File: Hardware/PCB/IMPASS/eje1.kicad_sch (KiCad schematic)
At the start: 18 parts, among them Q1 BC847BDW1, Q2 DMP3013SFV, Q3 DMP3013SFV, Q4 DMP3013SFV, Q5 BC847BDW1, Q6 DMP3013SFV, Q71 DMN3008SFG, Q73 DMN3008SFG, Q75 DMN3008SFG, Q77 DMN3008SFG

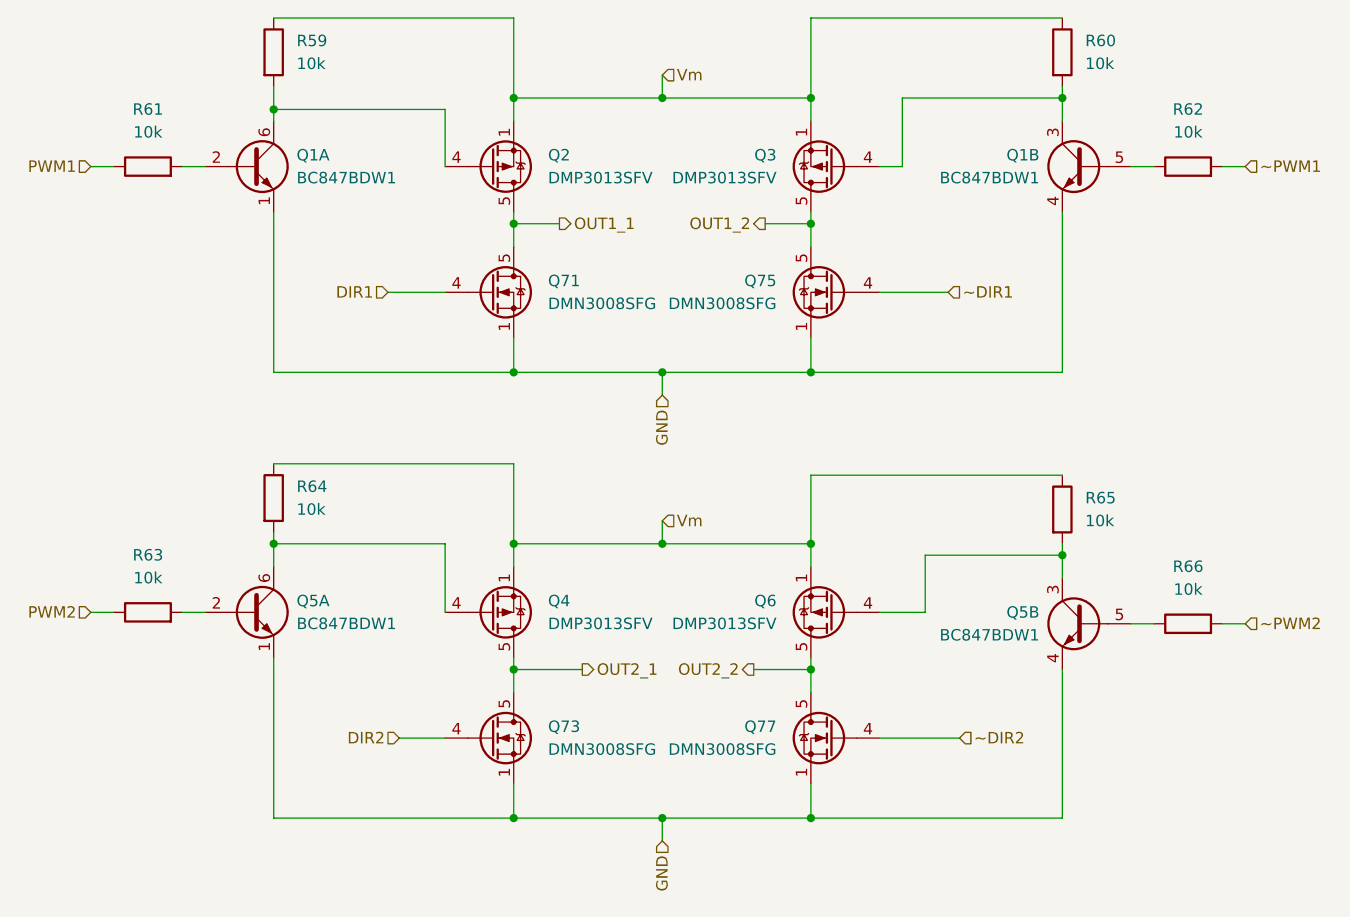
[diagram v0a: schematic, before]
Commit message: Hardware: Update all the logic pcb 	- added ads1015 	- added the logic foe P-MOSFET 	- added I2C connector
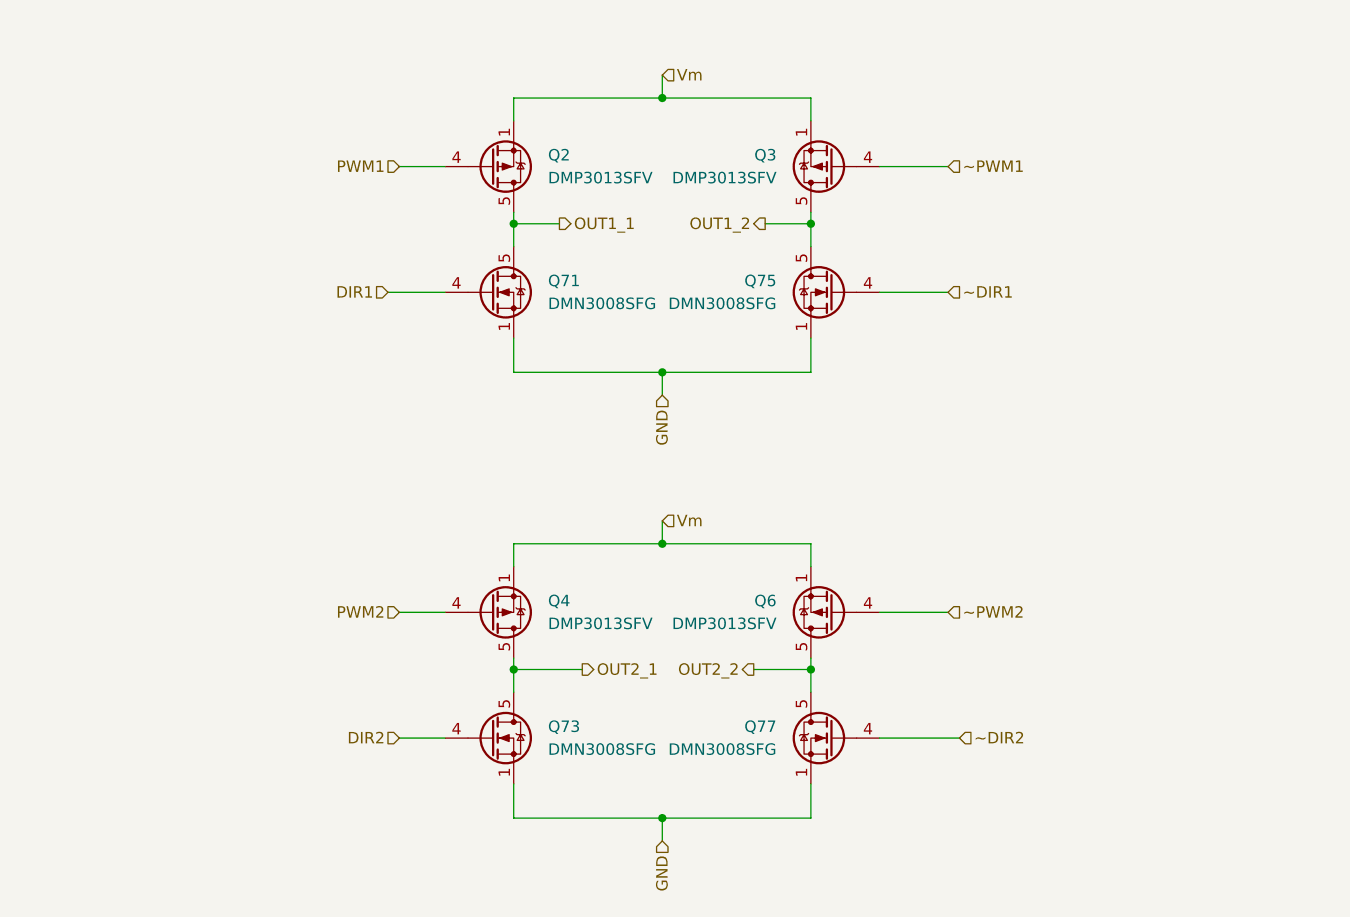
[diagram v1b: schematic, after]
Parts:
- removed Q1, Q5: BC847BDW1, Package_TO_SOT_SMD:SOT-363_SC-70-6, symbol Transistor_BJT:BC847BDW1
- removed R59, R60, R61, R62, R63, R64, R65, R66: 10k, Resistor_SMD:R_0603_1608Metric, symbol Device:R
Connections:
- net PWM1: now also Q2.4 (G)
- net PWM2: now also Q4.4 (G)
- net ~PWM1: now also Q3.4 (G)
- net ~PWM2: now also Q6.4 (G)
